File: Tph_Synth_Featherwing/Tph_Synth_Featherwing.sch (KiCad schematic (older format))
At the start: 0 parts

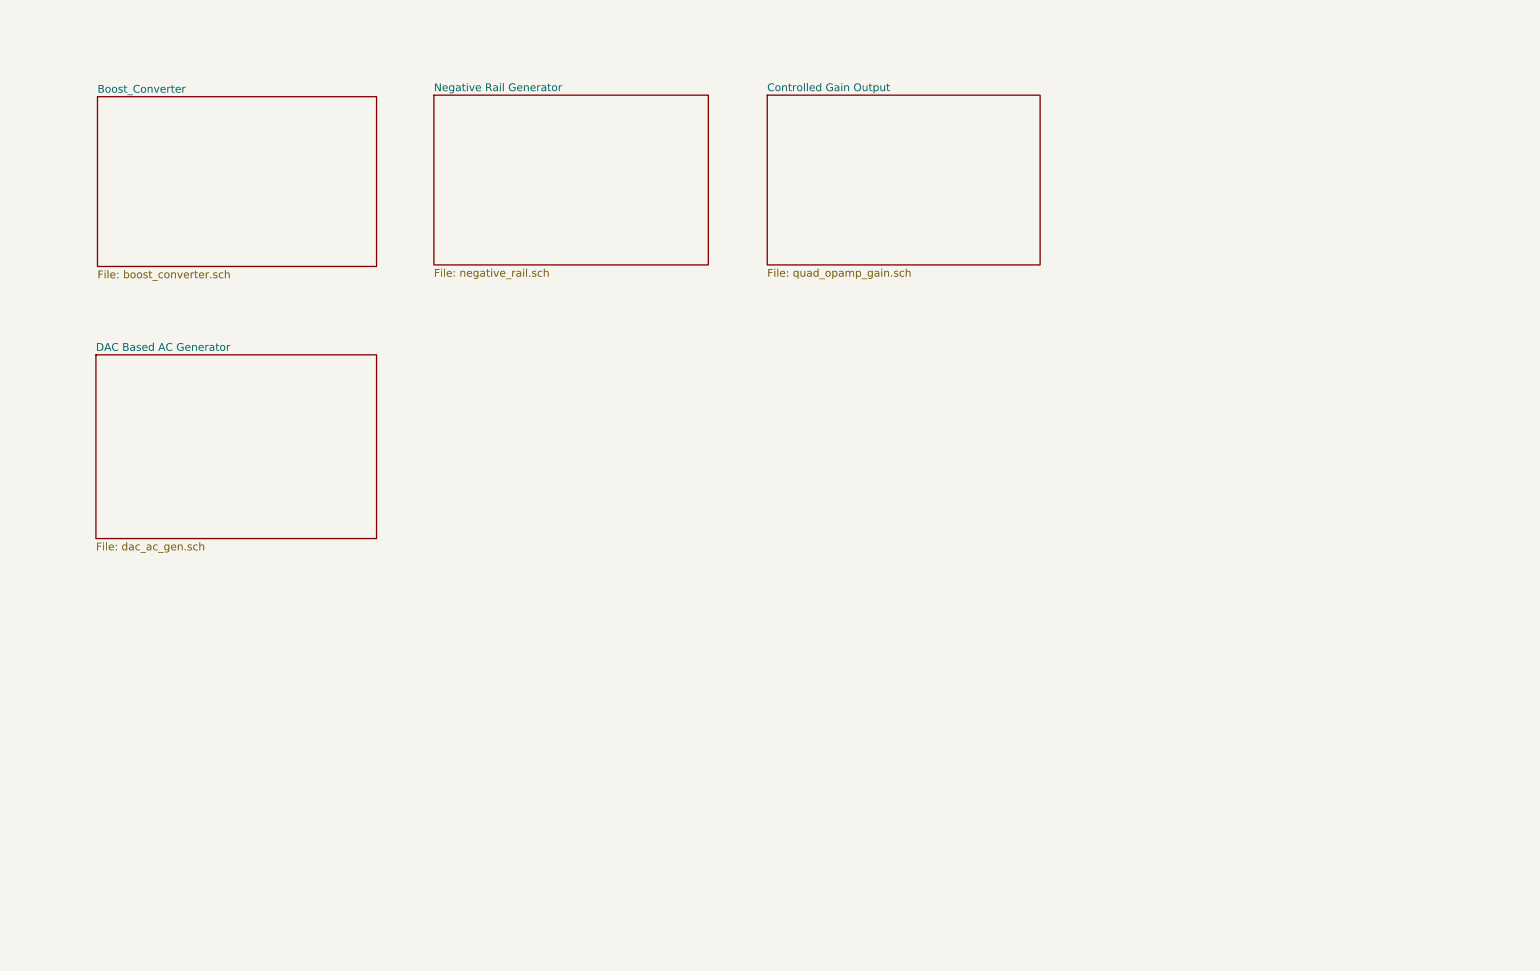
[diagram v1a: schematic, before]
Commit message: Add parts for DAC
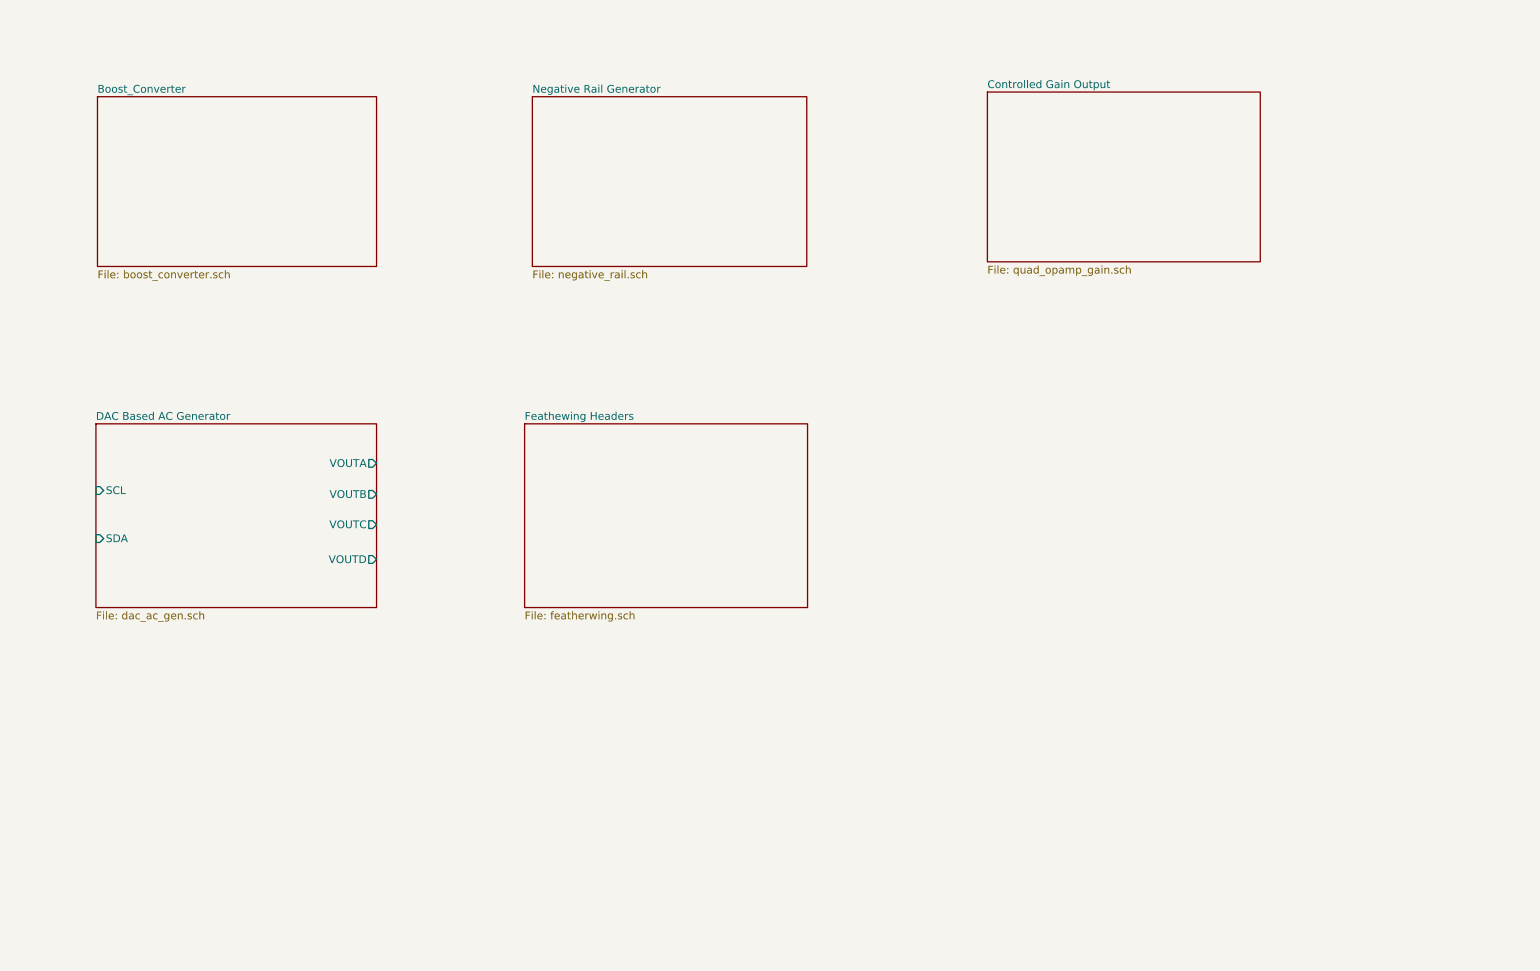
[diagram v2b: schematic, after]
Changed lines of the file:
@@
 $Descr A4 11693 8268
 encoding utf-8
-Sheet 1 5
+Sheet 1 6
 Title ""
 Date ""
@@
 $EndSheet
 $Sheet
-S 3555 1885 1770 1095
+S 4190 1895 1770 1095
 U 5DCBF5D4
 F0 "Negative Rail Generator" 50
@@
 $EndSheet
 $Sheet
-S 5705 1885 1760 1095
+S 7125 1865 1760 1095
 U 5DCBF60B
 F0 "Controlled Gain Output" 50
@@
 $EndSheet
 $Sheet
-S 1375 3560 1810 1185
+S 1375 4005 1810 1185
 U 5DCBF63F
 F0 "DAC Based AC Generator" 50
 F1 "dac_ac_gen.sch" 50
+F2 "VOUTA" O R 3185 4260 50
+F3 "VOUTB" O R 3185 4460 50
+F4 "VOUTC" O R 3185 4655 50
+F5 "VOUTD" O R 3185 4880 50
+F6 "SCL" I L 1375 4435 50
+F7 "SDA" I L 1375 4745 50
+$EndSheet
+$Sheet
+S 4140 4005 1825 1185
+U 5DECF7CD
+F0 "Feathewing Headers" 50
+F1 "featherwing.sch" 50
 $EndSheet
 $EndSCHEMATC

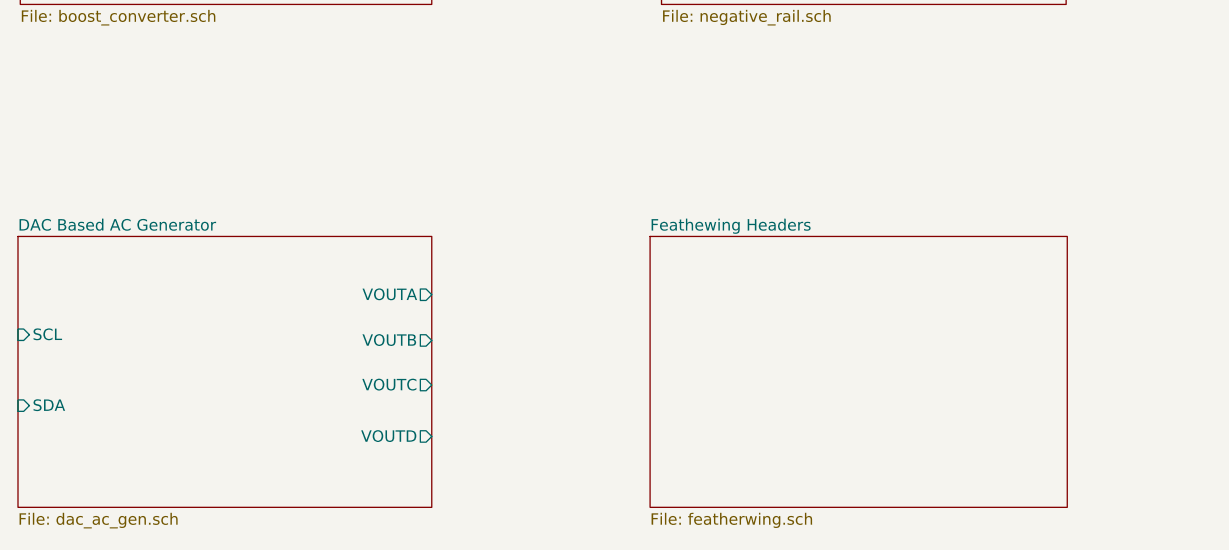
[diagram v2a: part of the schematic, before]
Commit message: Add parts for voltage inverter
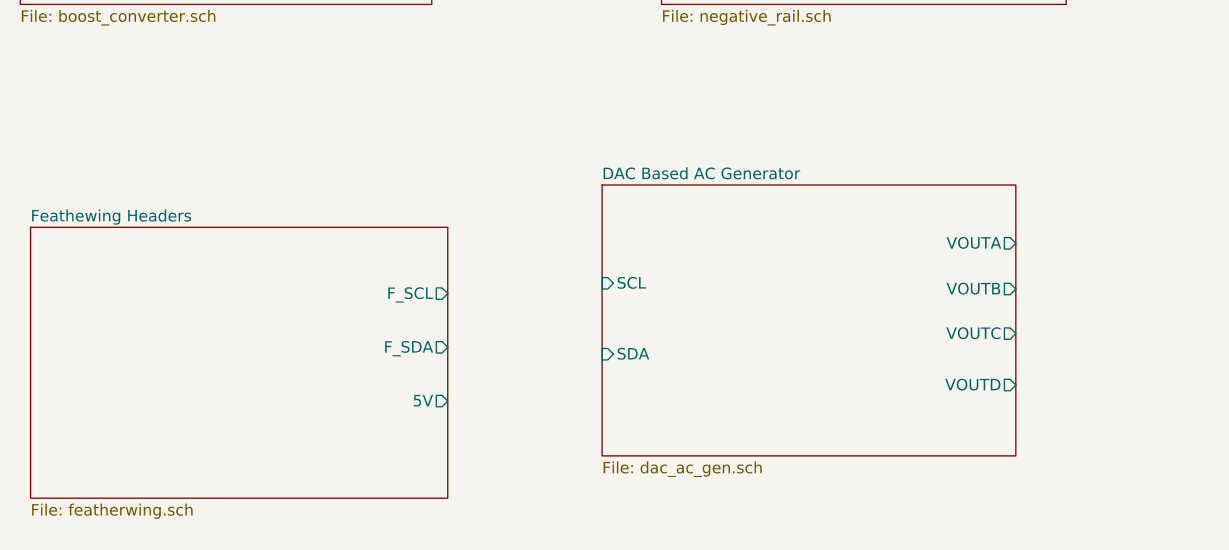
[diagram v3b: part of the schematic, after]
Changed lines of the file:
@@
 $EndSheet
 $Sheet
-S 1375 4005 1810 1185
+S 3930 3780 1810 1185
 U 5DCBF63F
 F0 "DAC Based AC Generator" 50
 F1 "dac_ac_gen.sch" 50
-F2 "VOUTA" O R 3185 4260 50
-F3 "VOUTB" O R 3185 4460 50
-F4 "VOUTC" O R 3185 4655 50
-F5 "VOUTD" O R 3185 4880 50
-F6 "SCL" I L 1375 4435 50
-F7 "SDA" I L 1375 4745 50
+F2 "VOUTA" O R 5740 4035 50
+F3 "VOUTB" O R 5740 4235 50
+F4 "VOUTC" O R 5740 4430 50
+F5 "VOUTD" O R 5740 4655 50
+F6 "SCL" I L 3930 4210 50
+F7 "SDA" I L 3930 4520 50
 $EndSheet
 $Sheet
-S 4140 4005 1825 1185
+S 1430 3965 1825 1185
 U 5DECF7CD
 F0 "Feathewing Headers" 50
 F1 "featherwing.sch" 50
+F2 "F_SCL" O R 3255 4255 50
+F3 "F_SDA" O R 3255 4490 50
+F4 "5V" O R 3255 4725 50
 $EndSheet
 $EndSCHEMATC

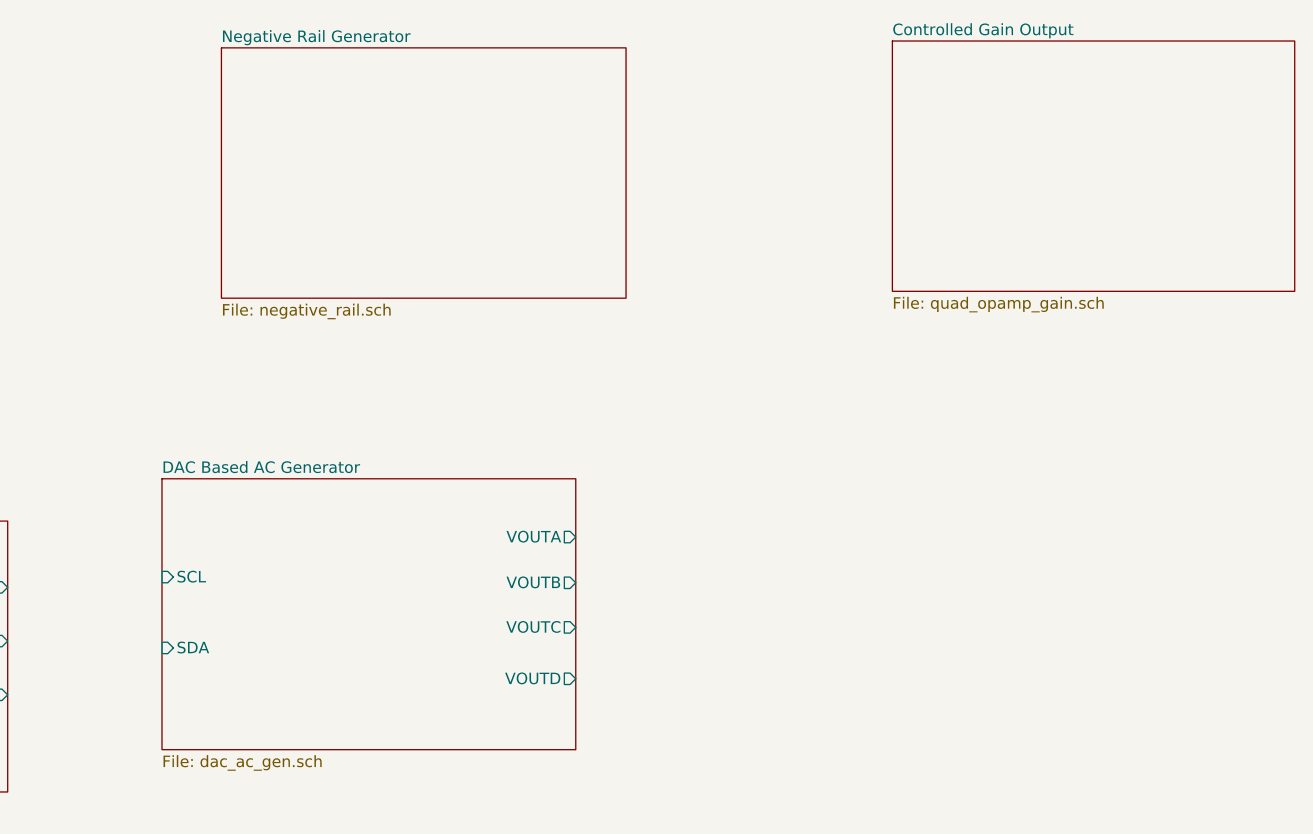
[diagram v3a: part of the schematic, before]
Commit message: Progress on sub-sheet labels and boost converter
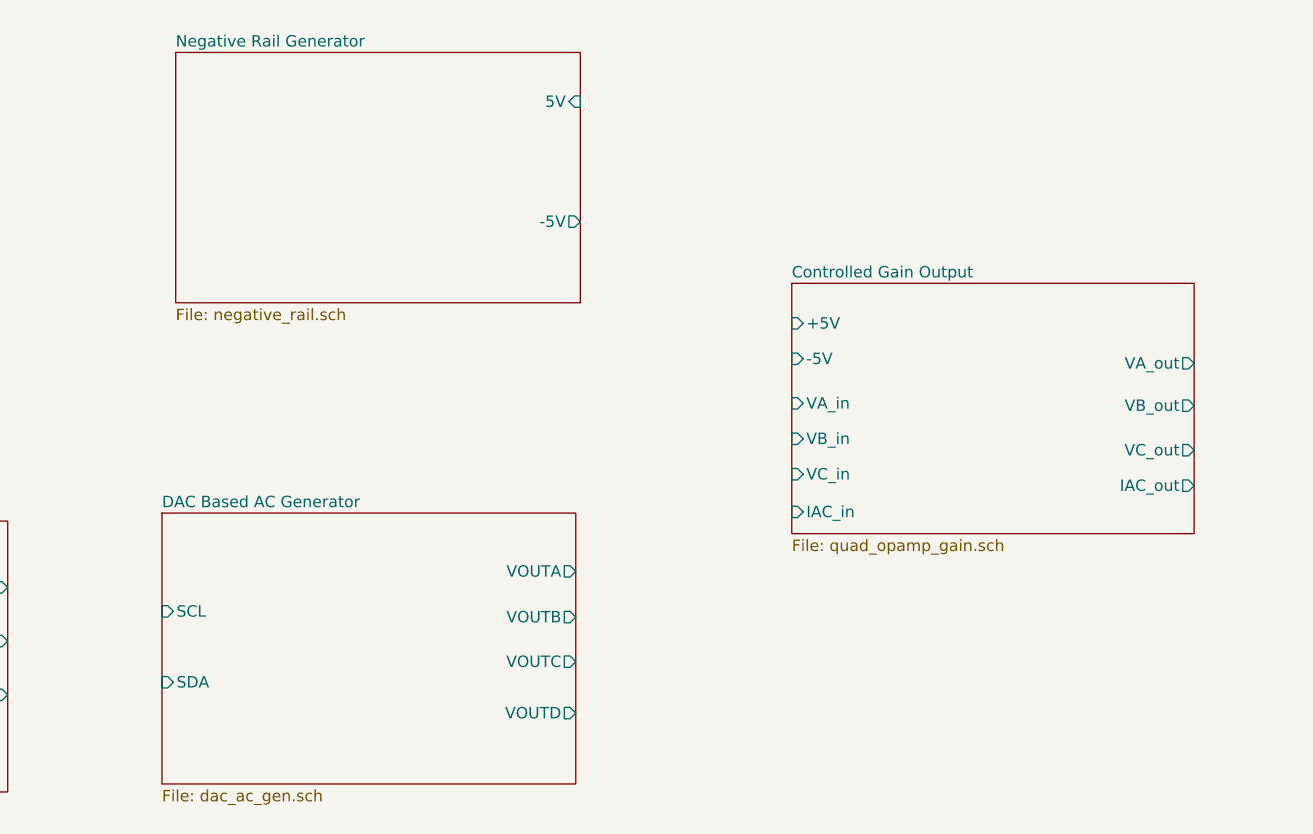
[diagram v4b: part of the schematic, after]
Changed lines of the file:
@@
 $EndSheet
 $Sheet
-S 4190 1895 1770 1095
+S 3990 1915 1770 1095
 U 5DCBF5D4
 F0 "Negative Rail Generator" 50
 F1 "negative_rail.sch" 50
+F2 "5V" I R 5760 2130 50
+F3 "-5V" O R 5760 2655 50
 $EndSheet
 $Sheet
-S 7125 1865 1760 1095
+S 6685 2925 1760 1095
 U 5DCBF60B
 F0 "Controlled Gain Output" 50
 F1 "quad_opamp_gain.sch" 50
+F2 "+5V" I L 6685 3100 50
+F3 "-5V" I L 6685 3255 50
+F4 "VA_out" O R 8445 3275 50
+F5 "VB_out" O R 8445 3460 50
+F6 "VC_out" O R 8445 3655 50
+F7 "IAC_out" O R 8445 3810 50
+F8 "VA_in" I L 6685 3450 50
+F9 "VB_in" I L 6685 3605 50
+F10 "VC_in" I L 6685 3760 50
+F11 "IAC_in" I L 6685 3925 50
 $EndSheet
 $Sheet
-S 3930 3780 1810 1185
+S 3930 3930 1810 1185
 U 5DCBF63F
 F0 "DAC Based AC Generator" 50
 F1 "dac_ac_gen.sch" 50
-F2 "VOUTA" O R 5740 4035 50
-F3 "VOUTB" O R 5740 4235 50
-F4 "VOUTC" O R 5740 4430 50
-F5 "VOUTD" O R 5740 4655 50
-F6 "SCL" I L 3930 4210 50
-F7 "SDA" I L 3930 4520 50
+F2 "VOUTA" O R 5740 4185 50
+F3 "VOUTB" O R 5740 4385 50
+F4 "VOUTC" O R 5740 4580 50
+F5 "VOUTD" O R 5740 4805 50
+F6 "SCL" I L 3930 4360 50
+F7 "SDA" I L 3930 4670 50
 $EndSheet
 $Sheet

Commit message: Boost-converter and inverting opamps
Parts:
- added J?: Conn_01x04, symbol Connector_Generic:Conn_01x04
- added J?: AudioJack3, symbol Connector:AudioJack3
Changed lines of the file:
@@
 $EndDescr
 $Sheet
-S 1385 1895 1800 1095
+S 1455 1955 1800 1095
 U 5DCBF5A8
 F0 "Boost_Converter" 50
 F1 "boost_converter.sch" 50
+F2 "VBAT" I L 1455 2305 50
+F3 "5V_OUT" O R 3255 2245 50
+F4 "VUSB" I L 1455 2720 50
 $EndSheet
 $Sheet
@@
 F2 "F_SCL" O R 3255 4255 50
 F3 "F_SDA" O R 3255 4490 50
-F4 "5V" O R 3255 4725 50
+F4 "VBAT" O L 1430 4405 50
+F5 "VUSB" O L 1430 4120 50
 $EndSheet
+$Comp
+L Connector_Generic:Conn_01x04 J?
+U 1 1 5DF7BE31
+P 9990 2315
+F 0 "J?" H 10070 2307 50  0000 L CNN
+F 1 "Conn_01x04" H 10070 2216 50  0000 L CNN
+F 2 "" H 9990 2315 50  0001 C CNN
+F 3 "~" H 9990 2315 50  0001 C CNN
+	1    9990 2315
+	1    0    0    -1
+$EndComp
+$Comp
+L Connector:AudioJack3 J?
+U 1 1 5DF7C0C6
+P 9930 3530
+F 0 "J?" H 9650 3463 50  0000 R CNN
+F 1 "AudioJack3" H 9650 3554 50  0000 R CNN
+F 2 "" H 9930 3530 50  0001 C CNN
+F 3 "~" H 9930 3530 50  0001 C CNN
+	1    9930 3530
+	-1   0    0    1
+$EndComp
 $EndSCHEMATC

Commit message: Added first-cut of schematic
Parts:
- gave numbers to parts that had none: 2
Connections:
- net labels added: GND
- wire segments 0 -> 46
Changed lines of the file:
@@
 $EndSheet
 $Comp
-L Connector_Generic:Conn_01x04 J?
+L Connector_Generic:Conn_01x04 J2
 U 1 1 5DF7BE31
-P 9990 2315
-F 0 "J?" H 10070 2307 50  0000 L CNN
-F 1 "Conn_01x04" H 10070 2216 50  0000 L CNN
-F 2 "" H 9990 2315 50  0001 C CNN
-F 3 "~" H 9990 2315 50  0001 C CNN
-	1    9990 2315
+P 10020 3035
+F 0 "J2" H 10100 3027 50  0000 L CNN
+F 1 "Conn_01x04" H 10100 2936 50  0000 L CNN
+F 2 "" H 10020 3035 50  0001 C CNN
+F 3 "~" H 10020 3035 50  0001 C CNN
+	1    10020 3035
 	1    0    0    -1
 $EndComp
 $Comp
-L Connector:AudioJack3 J?
+L Connector:AudioJack3 J1
 U 1 1 5DF7C0C6
-P 9930 3530
-F 0 "J?" H 9650 3463 50  0000 R CNN
-F 1 "AudioJack3" H 9650 3554 50  0000 R CNN
-F 2 "" H 9930 3530 50  0001 C CNN
-F 3 "~" H 9930 3530 50  0001 C CNN
-	1    9930 3530
+P 9955 4265
+F 0 "J1" H 9675 4198 50  0000 R CNN
+F 1 "AudioJack3" H 9675 4289 50  0000 R CNN
+F 2 "" H 9955 4265 50  0001 C CNN
+F 3 "~" H 9955 4265 50  0001 C CNN
+	1    9955 4265
 	-1   0    0    1
 $EndComp
+Wire Wire Line
+	9820 2935 8570 2935
+Wire Wire Line
+	8570 2935 8570 3275
+Wire Wire Line
+	8570 3275 8445 3275
+Wire Wire Line
+	8445 3460 8740 3460
+Wire Wire Line
+	8740 3460 8740 3035
+Wire Wire Line
+	8740 3035 9820 3035
+Wire Wire Line
+	9820 3135 8915 3135
+Wire Wire Line
+	8915 3135 8915 3655
+Wire Wire Line
+	8915 3655 8445 3655
+Wire Wire Line
+	9100 3810 8445 3810
+Wire Wire Line
+	9755 4165 9100 4165
+Wire Wire Line
+	9100 4165 9100 3810
+$Comp
+L power:GND #PWR08
+U 1 1 5DF77235
+P 9820 3235
+F 0 "#PWR08" H 9820 2985 50  0001 C CNN
+F 1 "GND" H 9825 3062 50  0000 C CNN
+F 2 "" H 9820 3235 50  0001 C CNN
+F 3 "" H 9820 3235 50  0001 C CNN
+	1    9820 3235
+	1    0    0    -1
+$EndComp
+$Comp
+L power:GND #PWR09
+U 1 1 5DF7740C
+P 9755 4365
+F 0 "#PWR09" H 9755 4115 50  0001 C CNN
+F 1 "GND" H 9760 4192 50  0000 C CNN
+F 2 "" H 9755 4365 50  0001 C CNN
+F 3 "" H 9755 4365 50  0001 C CNN
+	1    9755 4365
+	1    0    0    -1
+$EndComp
+Wire Wire Line
+	6685 3450 5875 3450
+Wire Wire Line
+	5875 3450 5875 4185
+Wire Wire Line
+	5875 4185 5740 4185
+Wire Wire Line
+	6085 3605 6685 3605
+Wire Wire Line
+	6085 3605 6085 4385
+Wire Wire Line
+	5740 4385 6085 4385
+Wire Wire Line
+	6685 3760 6290 3760
+Wire Wire Line
+	6290 3760 6290 4580
+Wire Wire Line
+	6290 4580 5740 4580
+Wire Wire Line
+	5740 4805 6490 4805
+Wire Wire Line
+	6490 4805 6490 3925
+Wire Wire Line
+	6685 3925 6490 3925
+Wire Wire Line
+	6145 2655 6145 3255
+Wire Wire Line
+	6145 2655 5760 2655
+Wire Wire Line
+	6685 3255 6145 3255
+Wire Wire Line
+	6685 3100 6280 3100
+Wire Wire Line
+	6280 3100 6280 2130
+Wire Wire Line
+	6280 2130 5760 2130
+Wire Wire Line
+	3255 2245 3555 2245
+Wire Wire Line
+	3555 2245 3555 1350
+Wire Wire Line
+	3555 1350 6280 1350
+Wire Wire Line
+	6280 1350 6280 2130
+Connection ~ 6280 2130
+Wire Wire Line
+	1430 4120 1165 4120
+Wire Wire Line
+	1165 4120 1165 2720
+Wire Wire Line
+	1165 2720 1455 2720
+Wire Wire Line
+	1455 2305 835  2305
+Wire Wire Line
+	835  2305 835  4405
+Wire Wire Line
+	835  4405 1430 4405
+Wire Wire Line
+	3930 4360 3460 4360
+Wire Wire Line
+	3460 4360 3460 4255
+Wire Wire Line
+	3460 4255 3255 4255
+Wire Wire Line
+	3255 4490 3470 4490
+Wire Wire Line
+	3470 4490 3470 4670
+Wire Wire Line
+	3470 4670 3930 4670
 $EndSCHEMATC

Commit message: Initial attempt at PCB
Signed-off-by: Tisham Dhar <whatnickd@gmail.com>
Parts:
- J1: footprint (none) -> Connector_Audio:Jack_3.5mm_CUI_SJ-3523-SMT_Horizontal
- J2: footprint (none) -> Connector_Molex:Molex_Nano-Fit_105314-xx04_2x02_P2.50mm_Horizontal
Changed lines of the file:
@@
 F 0 "J2" H 10100 3027 50  0000 L CNN
 F 1 "Conn_01x04" H 10100 2936 50  0000 L CNN
-F 2 "" H 10020 3035 50  0001 C CNN
+F 2 "Connector_Molex:Molex_Nano-Fit_105314-xx04_2x02_P2.50mm_Horizontal" H 10020 3035 50  0001 C CNN
 F 3 "~" H 10020 3035 50  0001 C CNN
 	1    10020 3035
@@
 F 0 "J1" H 9675 4198 50  0000 R CNN
 F 1 "AudioJack3" H 9675 4289 50  0000 R CNN
-F 2 "" H 9955 4265 50  0001 C CNN
+F 2 "Connector_Audio:Jack_3.5mm_CUI_SJ-3523-SMT_Horizontal" H 9955 4265 50  0001 C CNN
 F 3 "~" H 9955 4265 50  0001 C CNN
 	1    9955 4265

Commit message: Add blurb silk screen
Signed-off-by: Tisham Dhar <whatnickd@gmail.com>
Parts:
- added LOGO1: Logo_Open_Hardware_Small, Symbol:OSHW-Logo2_7.3x6mm_SilkScreen, symbol Graphic:Logo_Open_Hardware_Small
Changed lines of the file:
@@
 Wire Wire Line
 	3470 4670 3930 4670
+$Comp
+L Graphic:Logo_Open_Hardware_Small LOGO1
+U 1 1 5DFCD1ED
+P 7385 6865
+F 0 "LOGO1" H 7385 7140 50  0001 C CNN
+F 1 "Logo_Open_Hardware_Small" H 7385 6640 50  0001 C CNN
+F 2 "Symbol:OSHW-Logo2_7.3x6mm_SilkScreen" H 7385 6865 50  0001 C CNN
+F 3 "~" H 7385 6865 50  0001 C CNN
+	1    7385 6865
+	1    0    0    -1
+$EndComp
 $EndSCHEMATC
